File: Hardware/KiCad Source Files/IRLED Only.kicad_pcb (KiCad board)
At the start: 2 copper layers, 35 x 25 mm, 14 parts

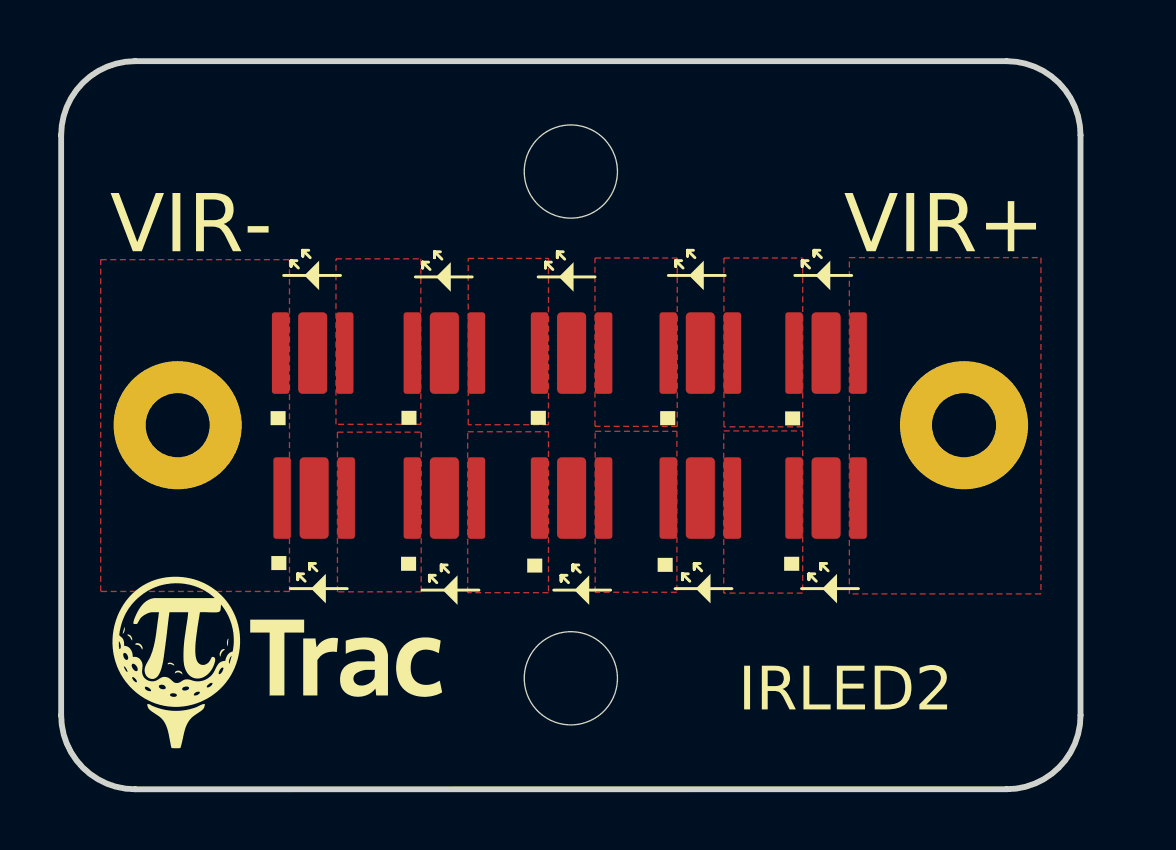
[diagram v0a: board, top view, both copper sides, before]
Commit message: IR LEDs: connect the VSMA1085400 center pad (second anode) on both LED boards
Vishay's package drawing (doc 80294) labels the VSMA1085400 pads Anode,
Anode, Cathode; the wide center pad under the die is an anode contact, not
an isolated thermal pad. The LED symbol was inherited from the earlier
Luminus SST-10-IRD (whose center pad is isolated), so pad 3 was left on an
isolated copper island and all strobe current went through the 0.35 mm
outer anode pad.

- Symbol: LED_ThermalPad -> VSMA1085400 (pin 3 named A, Vishay datasheet,
  description). D6-D15 pin 3 wired to pin 2; no-connect markers removed.
- PCB (IRLED Only, and the LED tab of V3 Connector + IRLED): pad 3 on the
  LED's anode net with a 2 mm bridge to pad 2. The gap to the cathode pad
  stays 0.3 mm. LED positions, holes and outline unchanged.
- Two anode nets were auto-renamed by the schematic (Net-(D11-A) ->
  Net-(D11-A-Pad2), Net-(D10-A) -> Net-(D9-K)); pours/pads renamed to match.
- Regenerated IRLED2 Only and V3 Connector + IRLED2 Gerbers and the
  schematic PDF (BOM/centroid unchanged).

ERC 0 (1 intended exclusion). DRC all three boards: 0 errors.

Co-Authored-By: Claude Opus 5.5 <noreply@anthropic.com>
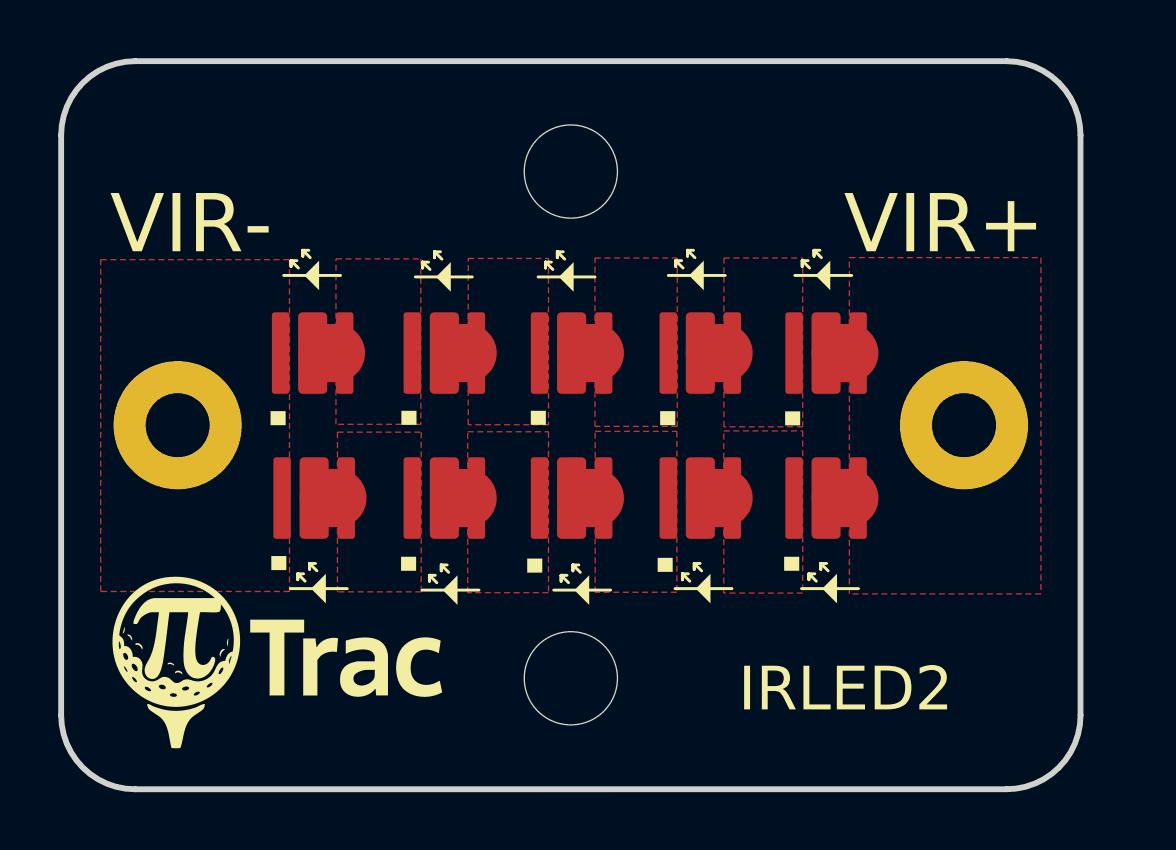
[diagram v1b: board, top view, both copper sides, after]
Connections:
- D10 pad 3: (no net) -> Net-(D10-A)
- D11 pad 3: (no net) -> Net-(D11-A)
- D12 pad 3: (no net) -> Net-(D11-K)
- D13 pad 3: (no net) -> Net-(D12-K)
- D14 pad 3: (no net) -> Net-(D13-K)
- D15 pad 3: (no net) -> Net-(D14-K)
- D6 pad 3: (no net) -> Net-(D11-A)
- D7 pad 3: (no net) -> Net-(D6-K)
- D8 pad 3: (no net) -> Net-(D7-K)
- D9 pad 3: (no net) -> Net-(D8-K)
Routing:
- net Net-(D11-A): track 0.00 -> 0.60 mm
